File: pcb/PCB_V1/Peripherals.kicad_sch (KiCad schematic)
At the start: 32 parts, among them J301 SHT4x / XH 2.50, J302 FLOAT / WAGO 2601, J401 Molex 104031-0811, U301 DS3231MZ+TRL

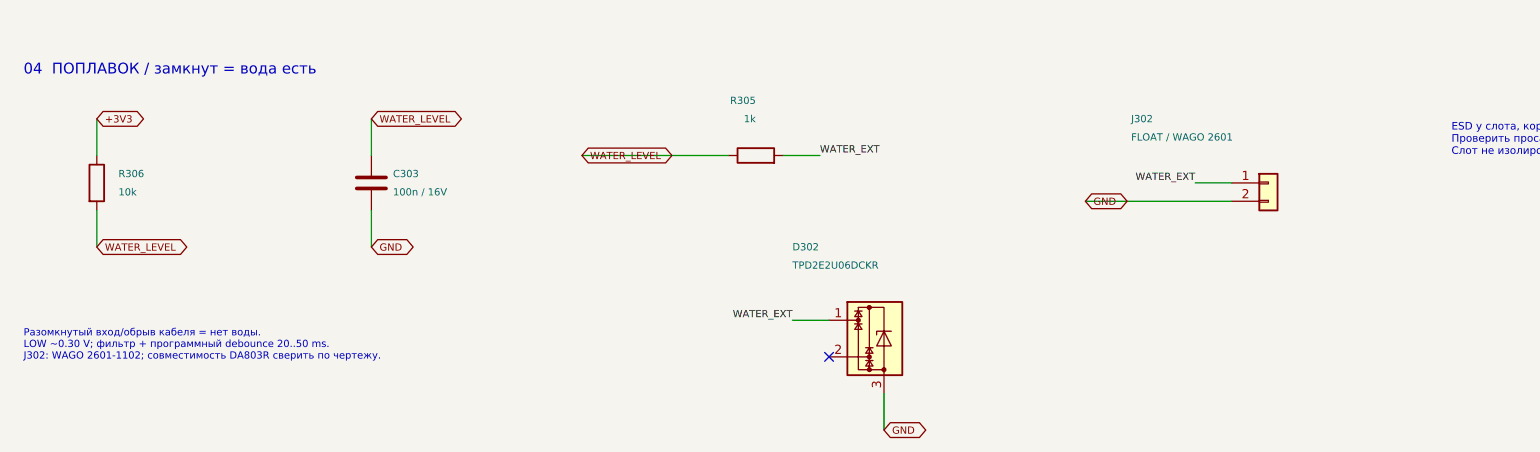
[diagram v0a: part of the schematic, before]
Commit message: pcb: move board to 24 V input with 12 V aux buck and merged LED bar channel
Revision 0.14 of PCB_V1 (see pcb/PCB_V1/REDESIGN_24V.md):
- 24 V input on keyed XT60PW-M (pin 1 GND, pin 2 +24V); LM74700, input
  MOSFET and F901 removed; SMBJ26CA TVS; 220 uF/50 V bulk
- ATM mini-blade fuses in XF-508P-B-B holders: F902 10 A loads, F903 7.5 A LED
- new LMR16020 24 V -> 12 V aux buck (500 kHz) feeding PC fans, the
  UCC27524A heater gate driver and the TPS54202 3.3 V buck; TPS70950 removed
- heater and pump on 24 V: SMBJ30A drain TVS, AO3422 + SS36 pump stage
- LED CH1 panel keeps SRP1770TA/0.027 R/1k, switch now CSD19534Q5A;
  CH2 drives both identical bars in parallel (J721 || J731, 0.40 R);
  third AL8853 channel removed
- TS-1187A buttons, DORABO/KANGNEX terminals
- project library: LMR16020 and CSD19534Q5A symbols, TI DQJ and XF-508P
  footprints
- verify_netlist.py / verify_board.py / analyze_*.py updated for 24 V;
  new sync_board.py updates the unrouted staging board from the netlist
- ERC 0/0; netlist, board and sizing checks pass; DRC only the 12 known
  ESP32 drill sizes plus unrouted connections; 163 components

Co-Authored-By: Claude Opus 5.5 <noreply@anthropic.com>
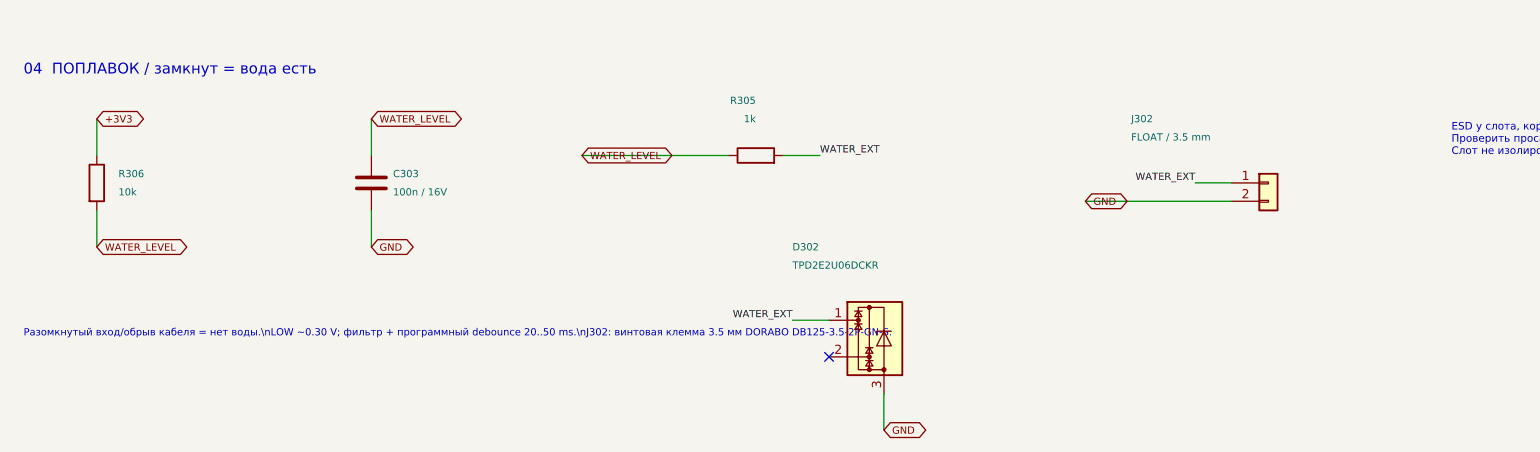
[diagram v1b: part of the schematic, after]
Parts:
- J302: value FLOAT / WAGO 2601 -> FLOAT / 3.5 mm; footprint TerminalBlock_WAGO:TerminalBlock_WAGO_2601-1102_1x02_P3.50mm_Horizontal -> TerminalBlock_Phoenix:TerminalBlock_Phoenix_PT-1,5-2-3.5-H_1x02_P3.50mm_Horizontal; LCSC (none) -> C466970; MPN (none) -> DB125-3.5-2P-GN-S; Manufacturer (none) -> DORABO
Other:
- note added: "Разомкнутый вход/обрыв кабеля = нет воды.\nLOW ~0.30 V; фильтр + программный debounce 20..50 ms.\nJ302: винтовая клемма 3.5 мм DORABO DB125-3.5-2P-GN-S."
- note removed: "Разомкнутый вход/обрыв кабеля = нет воды. LOW ~0.30 V; фильтр + программный debounce 20..50 ms. J302: WAGO 2601-1102; совместимость DA803R сверить по чертежу."
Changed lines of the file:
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@@
 		(comment 1 "Draft: input protection and LED drivers pending")
 	)
-	(text "Разомкнутый вход/обрыв кабеля = нет воды.\nLOW ~0.30 V; фильтр + программный debounce 20..50 ms.\nJ302: WAGO 2601-1102; совместимость DA803R сверить по чертежу."
+	(text "Разомкнутый вход/обрыв кабеля = нет воды.\\nLOW ~0.30 V; фильтр + программный debounce 20..50 ms.\\nJ302: винтовая клемма 3.5 мм DORABO DB125-3.5-2P-GN-S."
 		(exclude_from_sim no)
 		(at 20.32 268 0)
@@
 			)
 		)
-		(property "Value" "FLOAT / WAGO 2601"
+		(property "Value" "FLOAT / 3.5 mm"
 			(at 173.99 241.3 0)
 			(show_name no)
@@
 			)
 		)
-		(property "Footprint" "TerminalBlock_WAGO:TerminalBlock_WAGO_2601-1102_1x02_P3.50mm_Horizontal"
+		(property "Footprint" "TerminalBlock_Phoenix:TerminalBlock_Phoenix_PT-1,5-2-3.5-H_1x02_P3.50mm_Horizontal"
 			(at 193.04 247.65 0)
 			(hide yes)
@@
 			)
 		)
+		(property "LCSC" "C466970"
+			(at 193.04 247.65 0)
+			(effects
+				(font
+					(size 1 1)
+				)
+				(hide yes)
+				(justify left)
+			)
+		)
+		(property "MPN" "DB125-3.5-2P-GN-S"
+			(at 193.04 247.65 0)
+			(effects
+				(font
+					(size 1 1)
+				)
+				(hide yes)
+				(justify left)
+			)
+		)
+		(property "Manufacturer" "DORABO"
+			(at 193.04 247.65 0)
+			(effects
+				(font
+					(size 1 1)
+				)
+				(hide yes)
+				(justify left)
+			)
+		)
